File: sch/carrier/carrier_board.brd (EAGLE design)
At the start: 100 x 100 mm, 93 parts, among them CON1 SM03B-GHS-TB, CON2 SM03B-GHS-TB, Q1 SI7145, Q2 SI7145, Q3 SI7145, Q4 SIJ438DP, Q5 SIJ438DP, Q6 SIJ438DP, Q7 SIJ438DP, U1 LTV-355T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

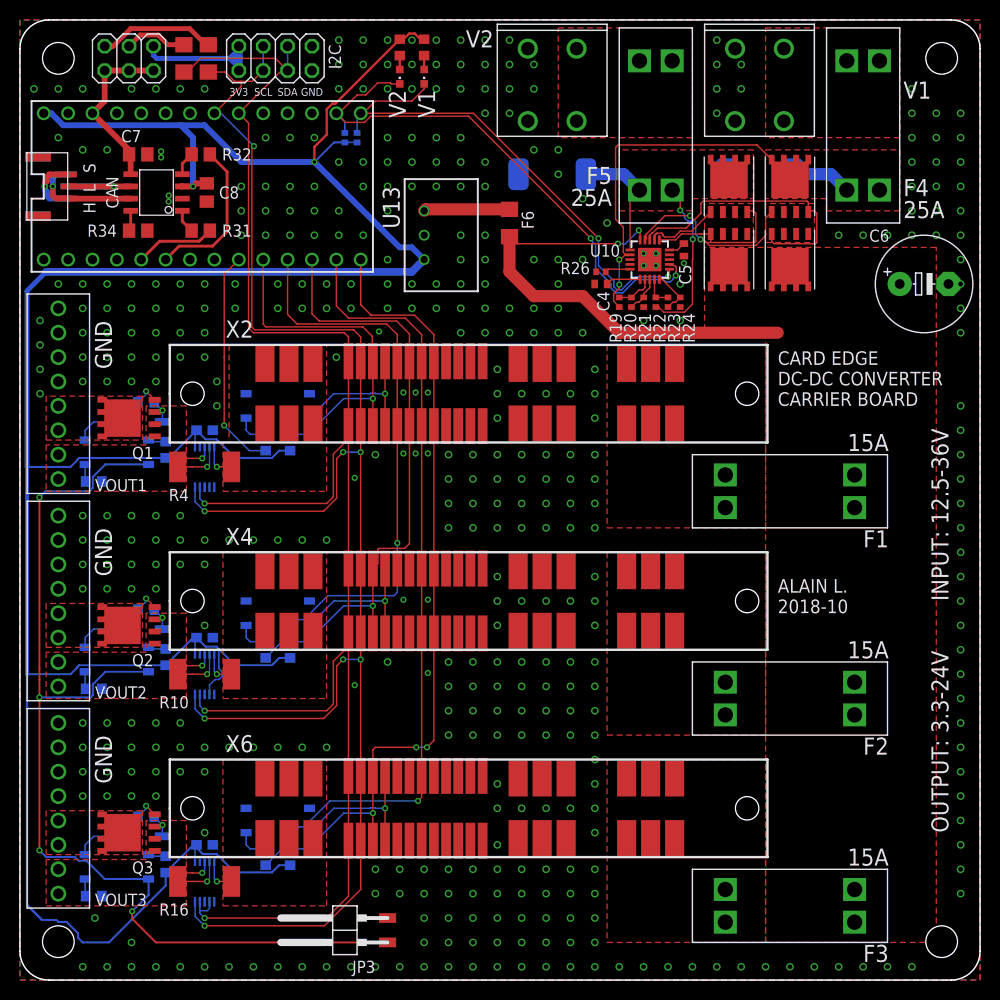
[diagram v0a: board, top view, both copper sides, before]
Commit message: Added carrier BOM; Chaned carrier MOSFETs
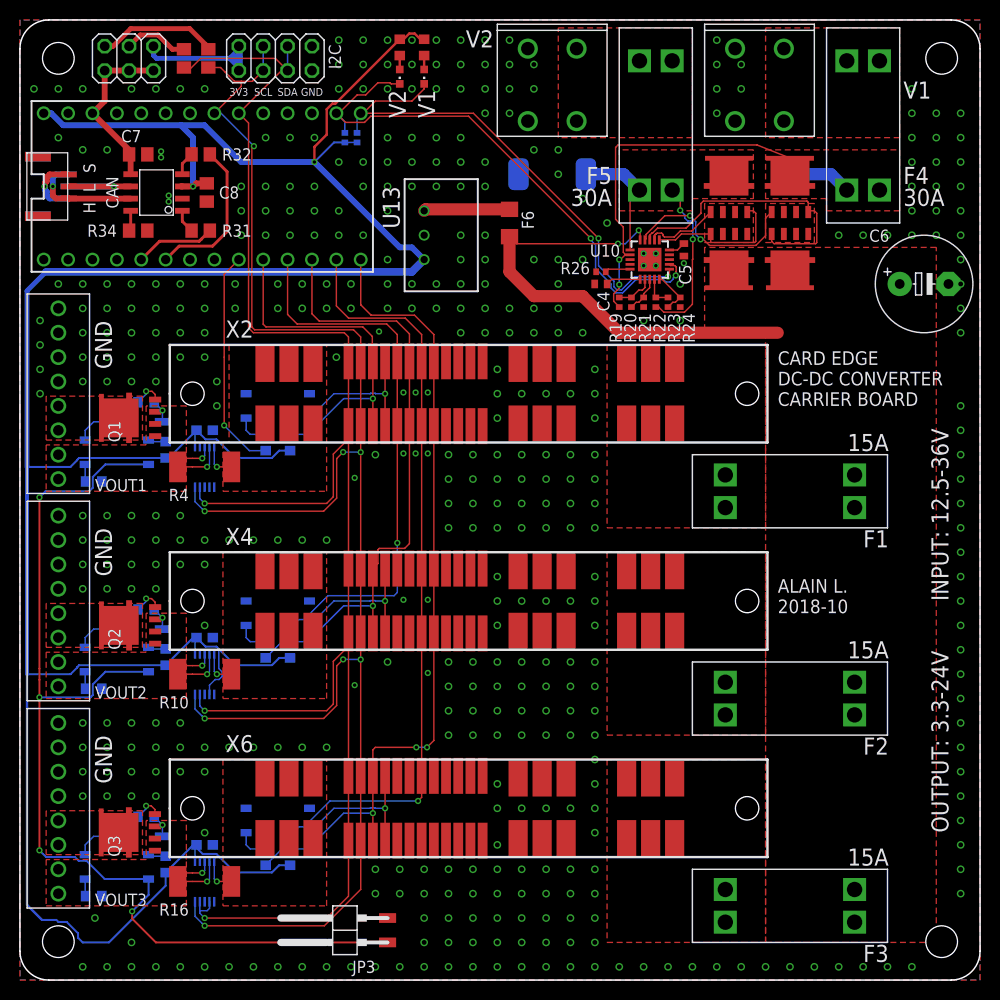
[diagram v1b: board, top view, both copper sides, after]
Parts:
- F4, F5: value 25A -> 30A
- Q1, Q2, Q3: device LTM4607:SO-8-POWERPAK -> LTM4607:POWERPAK_SO8L_SINGLE
- Q4, Q5, Q6, Q7: device LTM4607:TRANS_SIRA90DP-T1-GE3 -> LTM4607:POWERPAK_SO8L_SINGLE
- R19, R22: value 4M -> 4.12M
- R20, R23: value 227.1k -> 234k
- R21, R24: value 120.7k -> 124k
- R28, R29: device rcl:R1206 -> rcl:R0805
- R30, R33: value (none) -> 2k
- moved Q2 2.79 mm to (64.7, 86.4), turned to 90 degrees
- moved Q1 2.79 mm to (64.7, 108.0), turned to 90 degrees
- moved Q3 2.76 mm to (64.7, 64.8), turned to 90 degrees
- moved Q4 2.67 mm to (124.5, 129.4), turned to 0 degrees
- moved Q5 2.67 mm to (124.5, 127.1), turned to 180 degrees
- moved Q6 2.67 mm to (130.8, 129.4), turned to 0 degrees
- moved Q7 2.67 mm to (130.8, 127.1), turned to 180 degrees
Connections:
- net MCU_RUN1 renamed /MCU_RUN1
- net MCU_RUN2 renamed /MCU_RUN2
- net MCU_RUN3 renamed /MCU_RUN3
- net G1: now also Q6.P$4, Q7.P$4; no longer Q6.4, Q7.4
- net G2: now also Q4.P$4, Q5.P$4; no longer Q4.4, Q5.4
- net GATE_VOUT1: now also Q1.P$4; no longer Q1.4
- net GATE_VOUT2: now also Q2.P$4; no longer Q2.4
- net GATE_VOUT3: now also Q3.P$4; no longer Q3.4
- net V1: now also Q6.P$5, Q6.P$6, Q6.P$7, Q6.P$8; no longer Q6.5, Q6.6, Q6.7, Q6.8, Q6.9
- net V2: now also Q4.P$5, Q4.P$6, Q4.P$7, Q4.P$8; no longer Q4.5, Q4.6, Q4.7, Q4.8, Q4.9
- net VIN: now also Q5.P$5, Q5.P$6, Q5.P$7, Q5.P$8, Q7.P$5, Q7.P$6, Q7.P$7, Q7.P$8; no longer Q5.5, Q5.6, Q5.7, Q5.8, Q5.9, Q7.5, Q7.6, Q7.7, Q7.8, Q7.9
- net VOUT1: now also Q1.P$1, Q1.P$2, Q1.P$3; no longer Q1.1, Q1.2, Q1.3
- net VOUT2: now also Q2.P$1, Q2.P$2, Q2.P$3; no longer Q2.1, Q2.2, Q2.3
- net VOUT3: now also Q3.P$1, Q3.P$2, Q3.P$3; no longer Q3.1, Q3.2, Q3.3
- net VOUT_SWITCHED1: now also Q1.P$5, Q1.P$6, Q1.P$7, Q1.P$8; no longer Q1.5, Q1.6, Q1.7, Q1.8, Q1.P$1
- net VOUT_SWITCHED2: now also Q2.P$5, Q2.P$6, Q2.P$7, Q2.P$8; no longer Q2.5, Q2.6, Q2.7, Q2.8, Q2.P$1
- net VOUT_SWITCHED3: now also Q3.P$5, Q3.P$6, Q3.P$7, Q3.P$8; no longer Q3.5, Q3.6, Q3.7, Q3.8, Q3.P$1
- net VS1: now also Q6.P$1, Q6.P$2, Q6.P$3, Q7.P$1, Q7.P$2, Q7.P$3; no longer Q6.1, Q6.2, Q6.3, Q7.1, Q7.2, Q7.3
- net VS2: now also Q4.P$1, Q4.P$2, Q4.P$3, Q5.P$1, Q5.P$2, Q5.P$3; no longer Q4.1, Q4.2, Q4.3, Q5.1, Q5.2, Q5.3
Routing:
- net V1: track 42.1 -> 43.6 mm
